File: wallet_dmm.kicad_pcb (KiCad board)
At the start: 2 copper layers, 86 x 53 mm, 26 parts, among them J1 Conn_01x04, J2 Conn_01x02, Q1 T2N7002BK_LM, Q2 T2N7002BK_LM, SW1 RESET_BUTTON, SW2 BUTTON0, SW3 BUTTON1, SW4 BUTTON2, U1 STM32L051K8Tx, U2 TLC555xD, U3 MCP9700-E/TO

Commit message: Revision 2
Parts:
- added C10: 100nF, Capacitor_SMD:C_0603_1608Metric_Pad1.08x0.95mm_HandSolder, F.Cu at (155.4, 72.9)
- added C11: 100nF, Capacitor_SMD:C_0603_1608Metric_Pad1.08x0.95mm_HandSolder, F.Cu at (155.4, 78.2)
- added C9: 100nF, Capacitor_SMD:C_0603_1608Metric_Pad1.08x0.95mm_HandSolder, F.Cu at (155.3, 68.1)
- added J3: Conn_01x04, Connector_PinHeader_2.54mm:PinHeader_1x04_P2.54mm_Vertical, F.Cu at (96.0, 72.0)
- added J4: Voltmeter, Connector_PinHeader_2.54mm:PinHeader_1x02_P2.54mm_Vertical, F.Cu at (96.0, 86.5)
- added R10: 1M, Resistor_SMD:R_0603_1608Metric_Pad0.98x0.95mm_HandSolder, F.Cu at (98.8, 89.7)
- added R11: 1M, Resistor_SMD:R_0603_1608Metric_Pad0.98x0.95mm_HandSolder, F.Cu at (99.8, 84.0)
- added R4: 10k, Resistor_SMD:R_0603_1608Metric_Pad0.98x0.95mm_HandSolder, F.Cu at (111.6, 84.4)
- added R5: 100, Resistor_SMD:R_0603_1608Metric_Pad0.98x0.95mm_HandSolder, F.Cu at (148.5, 91.7)
- added R6: 4.7k, Resistor_SMD:R_0603_1608Metric_Pad0.98x0.95mm_HandSolder, F.Cu at (156.9, 68.2)
- added R7: 4.7k, Resistor_SMD:R_0603_1608Metric_Pad0.98x0.95mm_HandSolder, F.Cu at (157.0, 72.9)
- added R8: 4.7k, Resistor_SMD:R_0603_1608Metric_Pad0.98x0.95mm_HandSolder, F.Cu at (157.0, 78.1)
- added R9: 10M, Resistor_SMD:R_0603_1608Metric_Pad0.98x0.95mm_HandSolder, F.Cu at (98.8, 93.2)
- C1, C2, C3, C4, C5, C6, C7, C8: footprint Capacitor_SMD:C_1206_3216Metric_Pad1.33x1.80mm_HandSolder -> Capacitor_SMD:C_0603_1608Metric_Pad1.08x0.95mm_HandSolder
- J1: footprint project_specific_footprints:OLED_Header -> custom:OLED_Header
- J2: value Conn_01x02 -> Voltmeter; footprint project_specific_footprints:ADC_Connector -> Connector_PinHeader_2.54mm:PinHeader_1x02_P2.54mm_Vertical
- LED1: footprint project_specific_footprints:QBLP615-RGB-3053_QTB -> project:QBLP615-RGB-3053_QTB
- Q1, Q2: footprint project_specific_footprints:T2N7002BK -> project:T2N7002BK
- R1, R2: footprint Resistor_SMD:R_1206_3216Metric_Pad1.30x1.75mm_HandSolder -> Resistor_SMD:R_0603_1608Metric_Pad0.98x0.95mm_HandSolder
- R3: value 1kR -> 10k; footprint Resistor_SMD:R_1206_3216Metric_Pad1.30x1.75mm_HandSolder -> Resistor_SMD:R_0603_1608Metric_Pad0.98x0.95mm_HandSolder
- SPK1: footprint project_specific_footprints:XDCR_CPT-1117-83-SMT-TR -> project:XDCR_CPT-1117-83-SMT-TR
- SW1, SW2, SW3, SW4: footprint project_specific_footprints:SW4_PTS815 SJM 250 SMTR LFS_CNK -> project:SW4_PTS815 SJM 250 SMTR LFS_CNK
- V1: footprint project_specific_footprints:BK-870_CR1025_Holder -> custom:BK-870-TR
- moved SW1 95.4 mm to (155.9, 106.3)
- moved U3 88.8 mm to (162.5, 62.0), turned to 180 degrees
- moved J1 85.0 mm to (172.0, 97.2)
- moved SW2 79.8 mm to (161.0, 68.0), turned to 0 degrees
- moved Q1 79.1 mm to (148.5, 87.1), turned to 180 degrees
- moved SPK1 75.1 mm to (158.0, 91.0), turned to 180 degrees
- moved Q2 72.7 mm to (143.9, 87.1), turned to 180 degrees
- moved U2 63.8 mm to (151.0, 79.5), turned to 90 degrees
- moved SW4 60.9 mm to (161.0, 78.0), turned to 0 degrees
- moved R2 51.3 mm to (147.3, 80.8), turned to -90 degrees
- moved R1 48.3 mm to (147.3, 77.2), turned to -90 degrees
- moved V1 43.0 mm to (169.3, 107.0)
- moved C3 29.7 mm to (150.0, 84.1), turned to 180 degrees
- moved JP1 27.7 mm to (116.0, 77.7), turned to 90 degrees
- moved U1 27.2 mm to (118.0, 85.0)
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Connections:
- net BOOT0 renamed /BOOT0
- net I2C1_SCL renamed /I2C1_SCL
- net I2C1_SDA renamed /I2C1_SDA
- net LED_BLUE renamed /LED_BLUE
- net LED_GREEN renamed /LED_GREEN
- net LED_RED renamed /LED_RED
- net NRST renamed /NRST
- net OSC_OUT renamed /PIEZO_OUT
- net PIEZO_EN renamed /PIEZO_EN
- net TEMP_ADC renamed /TEMP_ADC
- net VDD renamed VCC
- J2 pad 1: ADC -> GND
- J2 pad 2: GND -> /CONTINUITY
- SW2 pad 1: BUTTON0 -> Net-(R6-Pad1)
- SW2 pad 2: BUTTON0 -> Net-(R6-Pad1)
- SW3 pad 1: BUTTON1 -> Net-(R7-Pad1)
- SW3 pad 2: BUTTON1 -> Net-(R7-Pad1)
- SW4 pad 1: BUTTON2 -> Net-(R8-Pad1)
- SW4 pad 2: BUTTON2 -> Net-(R8-Pad1)
- U1 pad 10: unconnected-(U1-PA4-Pad10) -> /CONTINUITY
- U1 pad 11: ADC -> /ADC
- U1 pad 21: BUTTON2 -> /BUTTON2
- U1 pad 22: BUTTON1 -> /BUTTON1
- U1 pad 23: BUTTON0 -> /BUTTON0
- U1 pad 24: unconnected-(U1-PA14-Pad24) -> /SWCLK
- U1 pad 25: unconnected-(U1-PA15-Pad25) -> /SWDIO
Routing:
- net /I2C1_SDA: track 22.0 -> 81.9 mm, vias 2 -> 4
- net /I2C1_SCL: track 20.2 -> 78.4 mm, vias 0 -> 4
- net BUTTON0: track 49.8 -> 0.00 mm, vias 4 -> 0
- net Net-(U2-CV): track 51.8 -> 2.69 mm, vias 4 -> 0
- net Net-(U2-THR): track 57.0 -> 13.0 mm, vias 4 -> 0
- net ADC: track 43.6 -> 0.00 mm, vias 4 -> 0
- net /BUTTON2: track 0.00 -> 43.0 mm, vias 0 -> 6
- net /CONTINUITY: track 0.00 -> 42.6 mm, vias 0 -> 2
- net /BUTTON1: track 0.00 -> 42.3 mm, vias 0 -> 4
- net /BUTTON0: track 0.00 -> 41.5 mm, vias 0 -> 4
- net BUTTON1: track 35.5 -> 0.00 mm
- net /SWCLK: track 0.00 -> 34.5 mm
- net VCC: track 194.0 -> 226.6 mm, vias 2 -> 10
- net /SWDIO: track 0.00 -> 31.2 mm
- net BUTTON2: track 26.2 -> 0.00 mm, vias 4 -> 0
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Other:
- board size 86 x 53 mm -> 85.5 x 54 mm
- board text removed: "NICHOLAS SARA | WALLET DMM | VERSION 1.0"

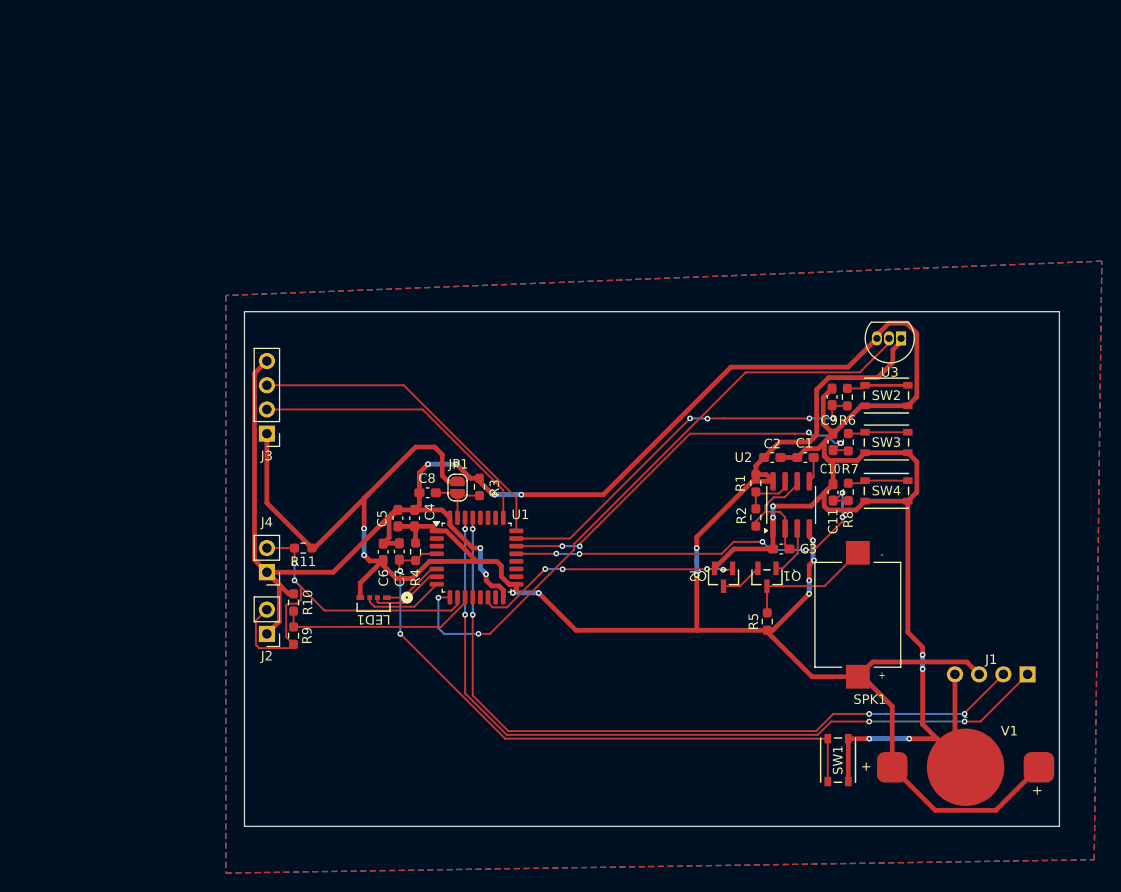
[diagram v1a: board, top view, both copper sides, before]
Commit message: Using ground plane vias.
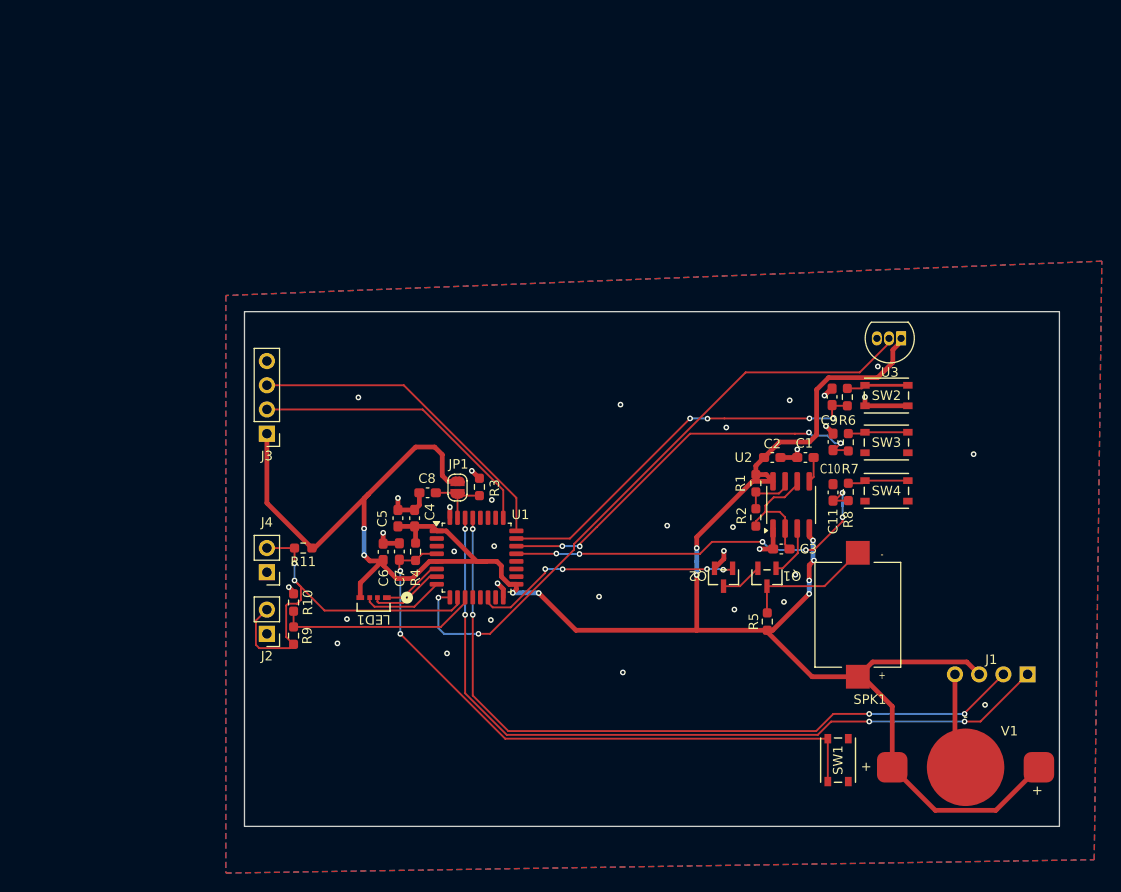
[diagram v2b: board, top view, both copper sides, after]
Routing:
- net GND: track 279.6 -> 39.0 mm, vias 12 -> 33
